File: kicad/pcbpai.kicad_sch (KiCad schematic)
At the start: 15 parts, among them J1 Fusible, J2 Conn_01x04_Pin, J3 Input 24 V, J4 Boton Encendido, J5 Parada de Emergencia, J6 Conn_01x06_Pin, J7 Raspberry GPIO, J8 Conn_01x09_Pin, SW1 SW_Push_DPDT, U6 ATtiny85-20P

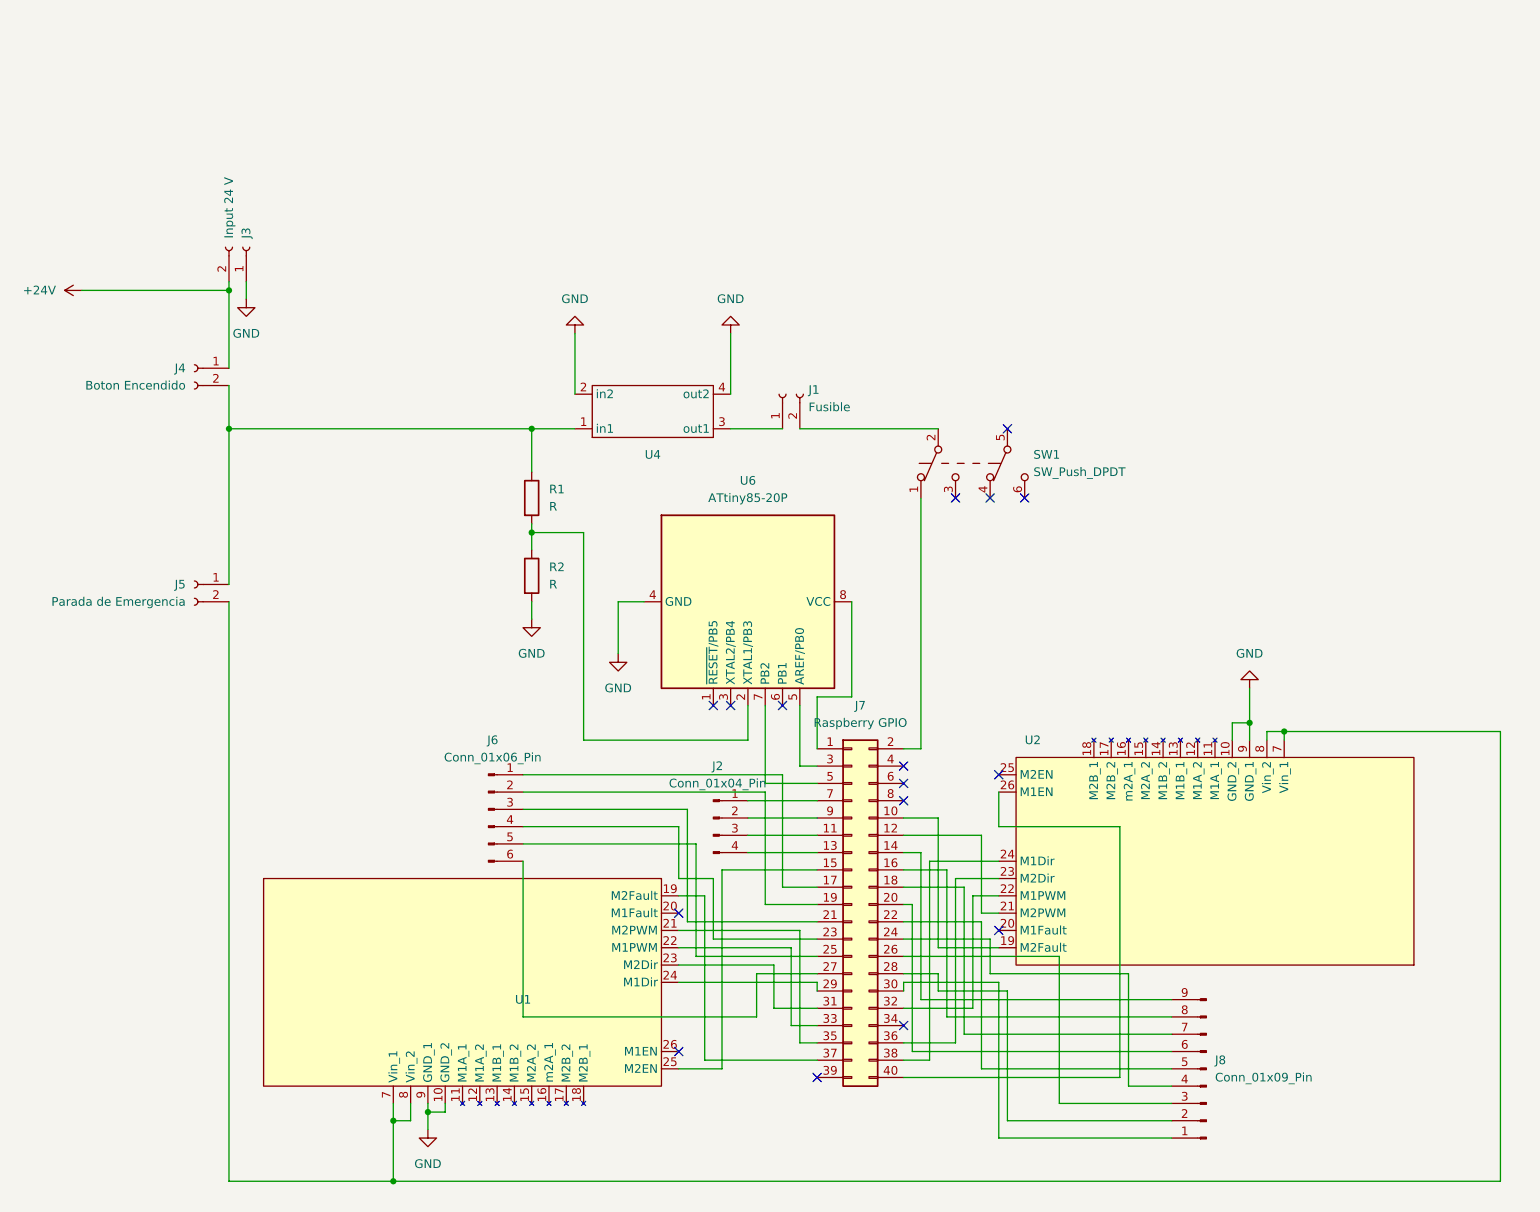
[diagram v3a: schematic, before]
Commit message: add termninal blocks for sensors and 24+ zone
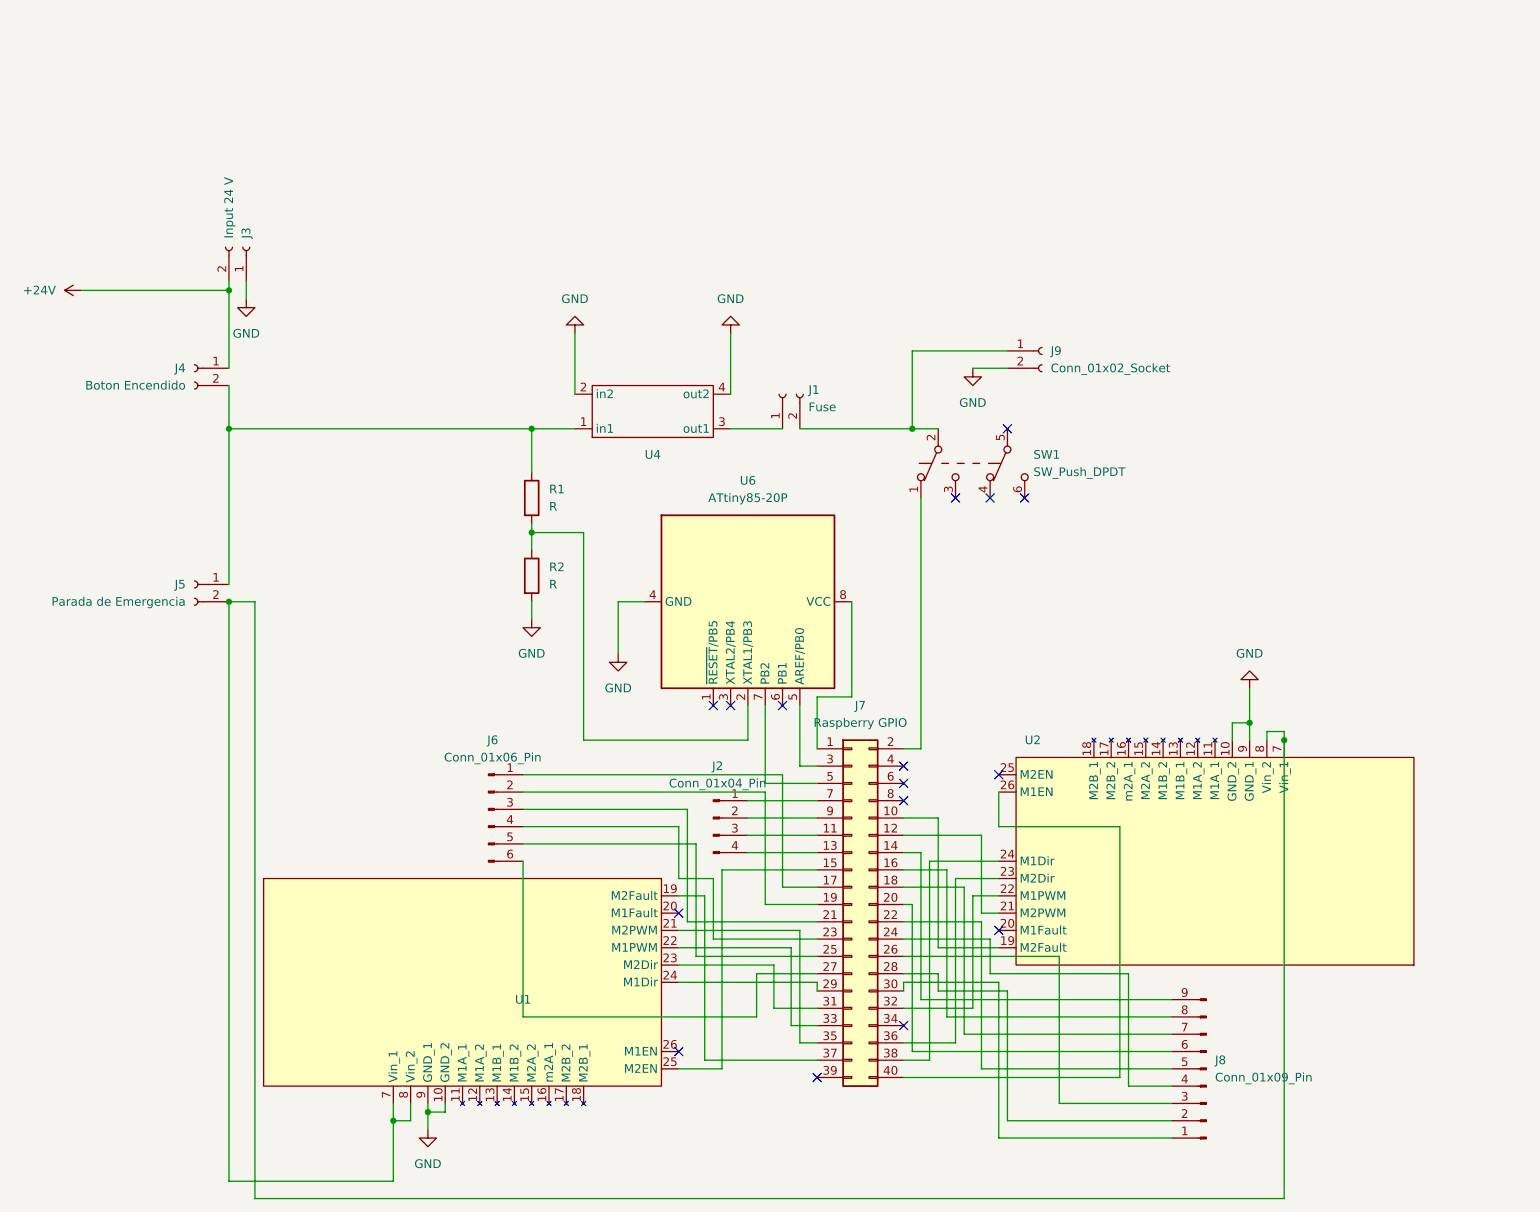
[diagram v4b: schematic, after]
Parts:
- added J9: Conn_01x02_Socket, TerminalBlock_Phoenix:TerminalBlock_Phoenix_PT-1,5-2-5.0-H_1x02_P5.00mm_Horizontal, symbol Connector:Conn_01x02_Socket
- J1: value Fusible -> Fuse; footprint PAI:fusible -> PAI:fuse
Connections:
- net GND: now also J9.2 (Pin_2)
- net at J1.2 (Pin_2), SW1.2 (B): now also J9.1 (Pin_1)
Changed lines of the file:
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@@
   (junction (at 101.6 52.07) (diameter 0) (color 0 0 0 0)
   )
+  (junction (at 212.09 97.79) (diameter 0) (color 0 0 0 0)
+  )
   (junction (at 57.15 52.07) (diameter 0) (color 0 0 0 0)
   )
-  (junction (at 81.28 162.56) (diameter 0) (color 0 0 0 0)
+  (junction (at 57.15 77.47) (diameter 0) (color 0 0 0 0)
   )
   (junction (at 57.15 31.75) (diameter 0) (color 0 0 0 0)
   )
+  (junction (at 157.48 52.07) (diameter 0) (color 0 0 0 0)
+  )
   (junction (at 81.28 153.67) (diameter 0) (color 0 0 0 0)
   )
@@
   )
   (junction (at 101.6 67.31) (diameter 0) (color 0 0 0 0)
-  )
-  (junction (at 212.09 96.52) (diameter 0) (color 0 0 0 0)
   )
   (no_connect (at 173.99 62.23))
@@
     (stroke (width 0) (type default))
   )
+  (wire (pts (xy 171.45 43.18) (xy 166.37 43.18))
+    (stroke (width 0) (type default))
+  )
   (wire (pts (xy 171.45 134.62) (xy 161.29 134.62))
     (stroke (width 0) (type default))
@@
     (stroke (width 0) (type default))
   )
+  (wire (pts (xy 157.48 52.07) (xy 161.29 52.07))
+    (stroke (width 0) (type default))
+  )
   (wire (pts (xy 101.6 52.07) (xy 101.6 58.42))
     (stroke (width 0) (type default))
@@
     (stroke (width 0) (type default))
   )
+  (wire (pts (xy 100.33 115.57) (xy 100.33 138.43))
+    (stroke (width 0) (type default))
+  )
+  (wire (pts (xy 187.96 110.49) (xy 187.96 147.32))
+    (stroke (width 0) (type default))
+  )
+  (wire (pts (xy 135.89 105.41) (xy 135.89 121.92))
+    (stroke (width 0) (type default))
+  )
+  (wire (pts (xy 170.18 156.21) (xy 170.18 133.35))
+    (stroke (width 0) (type default))
+  )
+  (wire (pts (xy 163.83 118.11) (xy 163.83 142.24))
+    (stroke (width 0) (type default))
+  )
+  (wire (pts (xy 156.21 99.06) (xy 158.75 99.06))
+    (stroke (width 0) (type default))
+  )
+  (wire (pts (xy 160.02 115.57) (xy 160.02 144.78))
+    (stroke (width 0) (type default))
+  )
+  (wire (pts (xy 168.91 132.08) (xy 168.91 127))
+    (stroke (width 0) (type default))
+  )
+  (wire (pts (xy 81.28 151.13) (xy 81.28 153.67))
+    (stroke (width 0) (type default))
+  )
+  (wire (pts (xy 143.51 133.35) (xy 143.51 134.62))
+    (stroke (width 0) (type default))
+  )
+  (wire (pts (xy 148.59 77.47) (xy 148.59 91.44))
+    (stroke (width 0) (type default))
+  )
+  (wire (pts (xy 143.51 91.44) (xy 143.51 99.06))
+    (stroke (width 0) (type default))
+  )
+  (wire (pts (xy 161.29 128.27) (xy 161.29 109.22))
+    (stroke (width 0) (type default))
+  )
+  (wire (pts (xy 209.55 96.52) (xy 212.09 96.52))
+    (stroke (width 0) (type default))
+  )
+  (wire (pts (xy 195.58 135.89) (xy 158.75 135.89))
+    (stroke (width 0) (type default))
+  )
+  (wire (pts (xy 135.89 92.71) (xy 135.89 104.14))
+    (stroke (width 0) (type default))
+  )
+  (wire (pts (xy 140.97 142.24) (xy 143.51 142.24))
+    (stroke (width 0) (type default))
+  )
+  (wire (pts (xy 130.81 46.99) (xy 130.81 38.1))
+    (stroke (width 0) (type default))
+  )
+  (wire (pts (xy 123.19 133.35) (xy 143.51 133.35))
+    (stroke (width 0) (type default))
+  )
+  (wire (pts (xy 171.45 40.64) (xy 157.48 40.64))
+    (stroke (width 0) (type default))
+  )
+  (wire (pts (xy 100.33 138.43) (xy 134.62 138.43))
+    (stroke (width 0) (type default))
+  )
+  (wire (pts (xy 100.33 110.49) (xy 123.19 110.49))
+    (stroke (width 0) (type default))
+  )
   (wire (pts (xy 158.75 62.23) (xy 158.75 99.06))
     (stroke (width 0) (type default))
   )
-  (wire (pts (xy 100.33 115.57) (xy 100.33 138.43))
-    (stroke (width 0) (type default))
-  )
-  (wire (pts (xy 187.96 110.49) (xy 187.96 147.32))
-    (stroke (width 0) (type default))
-  )
-  (wire (pts (xy 135.89 105.41) (xy 135.89 121.92))
-    (stroke (width 0) (type default))
-  )
-  (wire (pts (xy 170.18 156.21) (xy 170.18 133.35))
-    (stroke (width 0) (type default))
-  )
-  (wire (pts (xy 163.83 118.11) (xy 163.83 142.24))
-    (stroke (width 0) (type default))
-  )
-  (wire (pts (xy 156.21 99.06) (xy 158.75 99.06))
-    (stroke (width 0) (type default))
-  )
-  (wire (pts (xy 160.02 115.57) (xy 160.02 144.78))
-    (stroke (width 0) (type default))
-  )
-  (wire (pts (xy 168.91 132.08) (xy 168.91 127))
-    (stroke (width 0) (type default))
-  )
-  (wire (pts (xy 81.28 151.13) (xy 81.28 153.67))
-    (stroke (width 0) (type default))
-  )
-  (wire (pts (xy 143.51 133.35) (xy 143.51 134.62))
-    (stroke (width 0) (type default))
-  )
-  (wire (pts (xy 148.59 77.47) (xy 148.59 91.44))
-    (stroke (width 0) (type default))
-  )
-  (wire (pts (xy 143.51 91.44) (xy 143.51 99.06))
-    (stroke (width 0) (type default))
-  )
-  (wire (pts (xy 161.29 128.27) (xy 161.29 109.22))
-    (stroke (width 0) (type default))
-  )
-  (wire (pts (xy 209.55 96.52) (xy 212.09 96.52))
-    (stroke (width 0) (type default))
-  )
-  (wire (pts (xy 243.84 96.52) (xy 243.84 162.56))
-    (stroke (width 0) (type default))
-  )
-  (wire (pts (xy 195.58 135.89) (xy 158.75 135.89))
-    (stroke (width 0) (type default))
-  )
-  (wire (pts (xy 135.89 92.71) (xy 135.89 104.14))
-    (stroke (width 0) (type default))
-  )
-  (wire (pts (xy 140.97 142.24) (xy 143.51 142.24))
-    (stroke (width 0) (type default))
-  )
-  (wire (pts (xy 130.81 46.99) (xy 130.81 38.1))
-    (stroke (width 0) (type default))
-  )
-  (wire (pts (xy 123.19 133.35) (xy 143.51 133.35))
-    (stroke (width 0) (type default))
-  )
-  (wire (pts (xy 100.33 138.43) (xy 134.62 138.43))
-    (stroke (width 0) (type default))
-  )
-  (wire (pts (xy 100.33 110.49) (xy 123.19 110.49))
-    (stroke (width 0) (type default))
-  )
   (wire (pts (xy 204.47 95.25) (xy 207.01 95.25))
     (stroke (width 0) (type default))
@@
     (stroke (width 0) (type default))
   )
+  (wire (pts (xy 60.96 165.1) (xy 212.09 165.1))
+    (stroke (width 0) (type default))
+  )
   (wire (pts (xy 130.81 52.07) (xy 138.43 52.07))
     (stroke (width 0) (type default))
@@
     (stroke (width 0) (type default))
   )
+  (wire (pts (xy 212.09 165.1) (xy 212.09 97.79))
+    (stroke (width 0) (type default))
+  )
   (wire (pts (xy 86.36 152.4) (xy 86.36 154.94))
     (stroke (width 0) (type default))
@@
     (stroke (width 0) (type default))
   )
-  (wire (pts (xy 212.09 96.52) (xy 243.84 96.52))
-    (stroke (width 0) (type default))
-  )
   (wire (pts (xy 207.01 95.25) (xy 207.01 90.17))
     (stroke (width 0) (type default))
@@
     (stroke (width 0) (type default))
   )
-  (wire (pts (xy 81.28 162.56) (xy 243.84 162.56))
-    (stroke (width 0) (type default))
-  )
   (wire (pts (xy 161.29 128.27) (xy 170.18 128.27))
     (stroke (width 0) (type default))
@@
     (stroke (width 0) (type default))
   )
+  (wire (pts (xy 57.15 77.47) (xy 60.96 77.47))
+    (stroke (width 0) (type default))
+  )
   (wire (pts (xy 57.15 52.07) (xy 57.15 74.93))
     (stroke (width 0) (type default))
@@
     (stroke (width 0) (type default))
   )
+  (wire (pts (xy 60.96 77.47) (xy 60.96 165.1))
+    (stroke (width 0) (type default))
+  )
   (wire (pts (xy 133.35 111.76) (xy 143.51 111.76))
     (stroke (width 0) (type default))
@@
     (stroke (width 0) (type default))
   )
+  (wire (pts (xy 157.48 40.64) (xy 157.48 52.07))
+    (stroke (width 0) (type default))
+  )
   (wire (pts (xy 114.3 85.09) (xy 114.3 77.47))
     (stroke (width 0) (type default))
@@
     (stroke (width 0) (type default))
   )
-  (wire (pts (xy 140.97 52.07) (xy 161.29 52.07))
+  (wire (pts (xy 140.97 52.07) (xy 157.48 52.07))
     (stroke (width 0) (type default))
   )
@@
       (effects (font (size 1.27 1.27)) (justify right))
     )
-    (property "Value" "Fusible" (at 142.24 48.895 90)
+    (property "Value" "Fuse" (at 142.24 48.895 90)
       (effects (font (size 1.27 1.27)) (justify right))
     )
-    (property "Footprint" "PAI:fusible" (at 138.43 46.99 0)
+    (property "Footprint" "PAI:fuse" (at 138.43 46.99 0)
       (effects (font (size 1.27 1.27)) hide)
     )
@@
     )
   )
+  (symbol (lib_id "Connector:Conn_01x02_Socket") (at 176.53 40.64 0) (unit 1)
+    (in_bom yes) (on_board yes) (dnp no)
+    (property "Reference" "J9" (at 177.8 40.64 0)
+      (effects (font (size 1.27 1.27)) (justify left))
+    )
+    (property "Value" "Conn_01x02_Socket" (at 177.8 43.18 0)
+      (effects (font (size 1.27 1.27)) (justify left))
+    )
+    (property "Footprint" "TerminalBlock_Phoenix:TerminalBlock_Phoenix_PT-1,5-2-5.0-H_1x02_P5.00mm_Horizontal" (at 176.53 40.64 0)
+      (effects (font (size 1.27 1.27)) hide)
+    )
+    (property "Datasheet" "~" (at 176.53 40.64 0)
+      (effects (font (size 1.27 1.27)) hide)
+    )
+    (pin "1")
+    (pin "2")
+    (instances
+      (project "pcbpai"
+        (path "/f5990c61-1cb7-4f3a-8fd9-38b0012c8313"
+          (reference "J9") (unit 1)
+        )
+      )
+    )
+  )
   (symbol (lib_id "power:GND") (at 114.3 85.09 0) (unit 1)
     (in_bom yes) (on_board yes) (dnp no) (fields_autoplaced)
@@
         )
       )
+    )
+  )
+  (symbol (lib_id "power:GND") (at 166.37 43.18 0) (unit 1)
+    (in_bom yes) (on_board yes) (dnp no) (fields_autoplaced)
+    (property "Reference" "#PWR01" (at 166.37 49.53 0)
+      (effects (font (size 1.27 1.27)) hide)
+    )
+    (property "Value" "GND" (at 166.37 48.26 0)
+      (effects (font (size 1.27 1.27)))
+    )
+    (property "Footprint" "" (at 166.37 43.18 0)
+      (effects (font (size 1.27 1.27)) hide)
+    )
+    (property "Datasheet" "" (at 166.37 43.18 0)
+      (effects (font (size 1.27 1.27)) hide)
+    )
+    (pin "1")
+    (instances
+      (project "pcbpai"
+        (path "/f5990c61-1cb7-4f3a-8fd9-38b0012c8313"
+          (reference "#PWR01") (unit 1)
+        )
+      )

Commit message: finish pcb
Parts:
- removed J2: Conn_01x04_Pin, Connector_PinSocket_2.54mm:PinSocket_1x04_P2.54mm_Vertical, symbol Connector:Conn_01x04_Pin
- removed J6: Conn_01x06_Pin, Connector_PinSocket_2.54mm:PinSocket_1x06_P2.54mm_Vertical, symbol Connector:Conn_01x06_Pin
- removed J8: Conn_01x09_Pin, Connector_PinSocket_2.54mm:PinSocket_1x09_P2.54mm_Vertical, symbol Connector:Conn_01x09_Pin
- removed SW1: SW_Push_DPDT, PAI:switch, symbol Switch:SW_Push_DPDT
- removed U1, U2: ~, PAI:Pololu MAX 14870 Dual Shield Arduino, symbol Lib_PAI:Dual_MAX14870
- added D1, D2, D3, D4: ~, Connector_PinHeader_2.54mm:PinHeader_2x04_P2.54mm_Vertical, symbol Lib_PAI:Conector_2x4
- added J10, J11, J12, J8: Conn_01x02_Socket, Connector_Phoenix_MSTB:PhoenixContact_MSTBA_2,5_2-G_1x02_P5.00mm_Horizontal, symbol Connector:Conn_01x02_Socket
- added J2, J6: Conn_01x08_Socket, Connector_PinSocket_2.54mm:PinSocket_1x08_P2.54mm_Vertical, symbol Connector:Conn_01x08_Socket
- U4: footprint PAI:regulador -> PAI:regulator
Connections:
- net GND: now also J7.39 (Pin_39), D1.2 (GND), D2.2 (GND), D3.2 (GND), D4.2 (GND), J10.1 (Pin_1), J11.1 (Pin_1), J12.1 (Pin_1), J8.1 (Pin_1)
- net at J5.2 (Pin_2): now also J10.2 (Pin_2), J11.2 (Pin_2), J12.2 (Pin_2), J8.2 (Pin_2)
- net at J7.37 (Pin_37): now also D4.8 (PWML)
- net at J7.35 (Pin_35): now also D4.7 (PWMR)
- net at J7.33 (Pin_33): now also D4.5 (ER), D4.6 (EL)
- net at J7.31 (Pin_31): now also J2.1 (Pin_1)
- net at J7.29 (Pin_29): now also J2.2 (Pin_2)
- net at J7.15 (Pin_15): now also D3.8 (PWML)
- net at J7.12 (Pin_12): now also D1.5 (ER), D1.6 (EL)
- net at J7.32 (Pin_32): now also J6.7 (Pin_7)
- net at J7.36 (Pin_36): now also D2.5 (ER), D2.6 (EL)
- net at J7.38 (Pin_38): now also D2.7 (PWMR)
- net at J7.40 (Pin_40): now also D2.8 (PWML)
- net +3.3V: now reaches J7.1 (Pin_1), U6.8 (VCC)
- net +3.3V: now also D1.1 (Vin), D2.1 (Vin), D3.1 (Vin), D4.1 (Vin)
- net at J7.11 (Pin_11): now also D3.5 (ER), D3.6 (EL)
- net at J7.13 (Pin_13): now also D3.7 (PWMR)
- net at J7.16 (Pin_16): now also D1.7 (PWMR)
- net at J7.17 (Pin_17): now also J2.8 (Pin_8)
- net at J7.18 (Pin_18): now also D1.8 (PWML)
- net at J7.19 (Pin_19): now also J2.7 (Pin_7)
- net at J7.20 (Pin_20): now also J6.1 (Pin_1)
- net at J7.21 (Pin_21): now also J2.6 (Pin_6)
- net at J7.22 (Pin_22): now also J6.2 (Pin_2)
- net at J7.23 (Pin_23): now also J2.5 (Pin_5)
- net at J7.24 (Pin_24): now also J6.3 (Pin_3)
- net at J7.25 (Pin_25): now also J2.4 (Pin_4)
- net at J7.26 (Pin_26): now also J6.4 (Pin_4)
- net at J7.27 (Pin_27): now also J2.3 (Pin_3)
- net at J7.28 (Pin_28): now also J6.5 (Pin_5)
- net at J7.30 (Pin_30): now also J6.6 (Pin_6)
- net at J7.34 (Pin_34): now also J6.8 (Pin_8)
- no-connect marks 16 -> 19
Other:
- moved on the sheet: J1, J3, J4, J5, J7, J9, R1, R2, U4, U6

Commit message: add gerber files and change footprints
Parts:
- D1, D2, D3, D4: footprint Connector_PinHeader_2.54mm:PinHeader_2x04_P2.54mm_Vertical -> Connector_IDC:IDC-Header_2x05_P2.54mm_Vertical; symbol Lib_PAI:Conector_2x4 -> Lib_PAI:BTS7960_control_pins
- J7: footprint Connector_PinHeader_2.54mm:PinHeader_2x20_P2.54mm_Vertical -> Connector_IDC:IDC-Header_2x20_P2.54mm_Vertical
- U4: symbol Lib_PAI:Regulador -> Lib_PAI:Regulator
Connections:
- net +3.3V: now also D1.7 (VCC), D2.7 (VCC), D3.7 (VCC), D4.7 (VCC); no longer D1.1 (Vin), D2.1 (Vin), D3.1 (Vin), D4.1 (Vin)
- net GND: now also D1.8 (GND), D2.8 (GND), D3.8 (GND), D4.8 (GND); no longer D1.2 (GND), D2.2 (GND), D3.2 (GND), D4.2 (GND)
- net at D1.3 (R_EN): now also D1.4 (L_EN), J7.12 (Pin_12)
- net at J7.16 (Pin_16): now also D1.1 (RPWM); no longer D1.7 (PWMR)
- net at J7.18 (Pin_18): now also D1.2 (LPWM); no longer D1.8 (PWML)
- net at D2.3 (R_EN): now also D2.4 (L_EN), J7.36 (Pin_36)
- net at J7.38 (Pin_38): now also D2.1 (RPWM); no longer D2.7 (PWMR)
- net at J7.40 (Pin_40): now also D2.2 (LPWM); no longer D2.8 (PWML)
- net at J7.13 (Pin_13): now also D3.1 (RPWM); no longer D3.7 (PWMR)
- net at J7.15 (Pin_15): now also D3.2 (LPWM); no longer D3.8 (PWML)
- net at J7.35 (Pin_35): now also D4.1 (RPWM); no longer D4.7 (PWMR)
- net at J7.37 (Pin_37): now also D4.2 (LPWM); no longer D4.8 (PWML)
- net at D4.3 (R_EN): now also D4.4 (L_EN), J7.33 (Pin_33)
- net at D3.3 (R_EN): now also D3.4 (L_EN), J7.11 (Pin_11)
- now unconnected: D1.5 (ER), D1.6 (EL), D2.5 (ER), D2.6 (EL), D3.5 (ER), D3.6 (EL), D4.5 (ER), D4.6 (EL)
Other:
- moved on the sheet: J1, J10, J11, J12, J2, J3, J4, J5, J6, J7, J8, J9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
